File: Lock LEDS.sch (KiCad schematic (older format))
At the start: 9 parts

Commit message: Schematic completed first draft
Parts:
- R? (x3): value 510 -> 1.8k
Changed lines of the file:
@@
 $Descr A4 11693 8268
 encoding utf-8
-Sheet 3 12
+Sheet 3 18
 Title ""
 Date ""
@@
 P 4050 3250
 F 0 "R?" V 3843 3250 50  0000 C CNN
-F 1 "510" V 3934 3250 50  0000 C CNN
+F 1 "1.8k" V 3934 3250 50  0000 C CNN
 F 2 "" V 3980 3250 50  0001 C CNN
 F 3 "~" H 4050 3250 50  0001 C CNN
@@
 P 4050 3750
 F 0 "R?" V 3843 3750 50  0000 C CNN
-F 1 "510" V 3934 3750 50  0000 C CNN
+F 1 "1.8k" V 3934 3750 50  0000 C CNN
 F 2 "" V 3980 3750 50  0001 C CNN
 F 3 "~" H 4050 3750 50  0001 C CNN
@@
 P 4050 4250
 F 0 "R?" V 3843 4250 50  0000 C CNN
-F 1 "510" V 3934 4250 50  0000 C CNN
+F 1 "1.8k" V 3934 4250 50  0000 C CNN
 F 2 "" V 3980 4250 50  0001 C CNN
 F 3 "~" H 4050 4250 50  0001 C CNN

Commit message: Fixed PISO Shift Register Wiring
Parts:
- D? (x3): footprint (none) -> LED_SMD:LED_1206_3216Metric_ReverseMount_Hole1.8x2.4mm
- R? (x3): footprint (none) -> Resistor_SMD:R_1206_3216Metric_Pad1.42x1.75mm_HandSolder
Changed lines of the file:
@@
 F 0 "D?" H 4743 2995 50  0000 C CNN
 F 1 "NUM LOCK" H 4743 3086 50  0000 C CNN
-F 2 "" H 4750 3250 50  0001 C CNN
+F 2 "LED_SMD:LED_1206_3216Metric_ReverseMount_Hole1.8x2.4mm" H 4750 3250 50  0001 C CNN
 F 3 "~" H 4750 3250 50  0001 C CNN
 	1    4750 3250
@@
 F 0 "D?" H 4743 3495 50  0000 C CNN
 F 1 "CAPS LOCK" H 4743 3586 50  0000 C CNN
-F 2 "" H 4750 3750 50  0001 C CNN
+F 2 "LED_SMD:LED_1206_3216Metric_ReverseMount_Hole1.8x2.4mm" H 4750 3750 50  0001 C CNN
 F 3 "~" H 4750 3750 50  0001 C CNN
 	1    4750 3750
@@
 F 0 "D?" H 4743 3995 50  0000 C CNN
 F 1 "SCROLL LOCK" H 4743 4086 50  0000 C CNN
-F 2 "" H 4750 4250 50  0001 C CNN
+F 2 "LED_SMD:LED_1206_3216Metric_ReverseMount_Hole1.8x2.4mm" H 4750 4250 50  0001 C CNN
 F 3 "~" H 4750 4250 50  0001 C CNN
 	1    4750 4250
@@
 F 0 "R?" V 3843 3250 50  0000 C CNN
 F 1 "1.8k" V 3934 3250 50  0000 C CNN
-F 2 "" V 3980 3250 50  0001 C CNN
+F 2 "Resistor_SMD:R_1206_3216Metric_Pad1.42x1.75mm_HandSolder" V 3980 3250 50  0001 C CNN
 F 3 "~" H 4050 3250 50  0001 C CNN
 	1    4050 3250
@@
 F 0 "R?" V 3843 3750 50  0000 C CNN
 F 1 "1.8k" V 3934 3750 50  0000 C CNN
-F 2 "" V 3980 3750 50  0001 C CNN
+F 2 "Resistor_SMD:R_1206_3216Metric_Pad1.42x1.75mm_HandSolder" V 3980 3750 50  0001 C CNN
 F 3 "~" H 4050 3750 50  0001 C CNN
 	1    4050 3750
@@
 F 0 "R?" V 3843 4250 50  0000 C CNN
 F 1 "1.8k" V 3934 4250 50  0000 C CNN
-F 2 "" V 3980 4250 50  0001 C CNN
+F 2 "Resistor_SMD:R_1206_3216Metric_Pad1.42x1.75mm_HandSolder" V 3980 4250 50  0001 C CNN
 F 3 "~" H 4050 4250 50  0001 C CNN
 	1    4050 4250

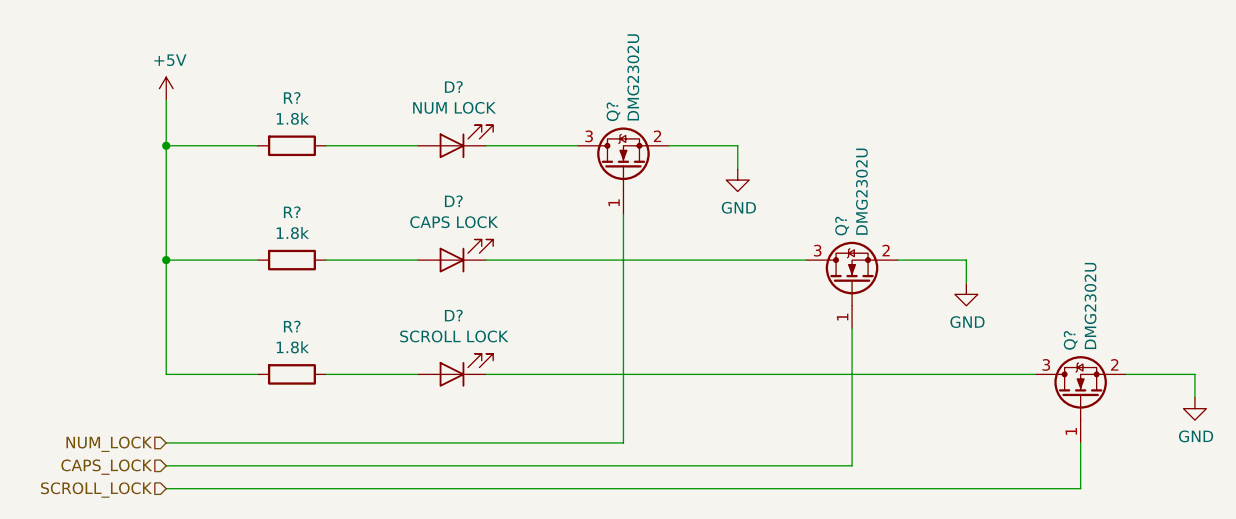
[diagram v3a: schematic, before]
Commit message: Corrected errors found in design rule check
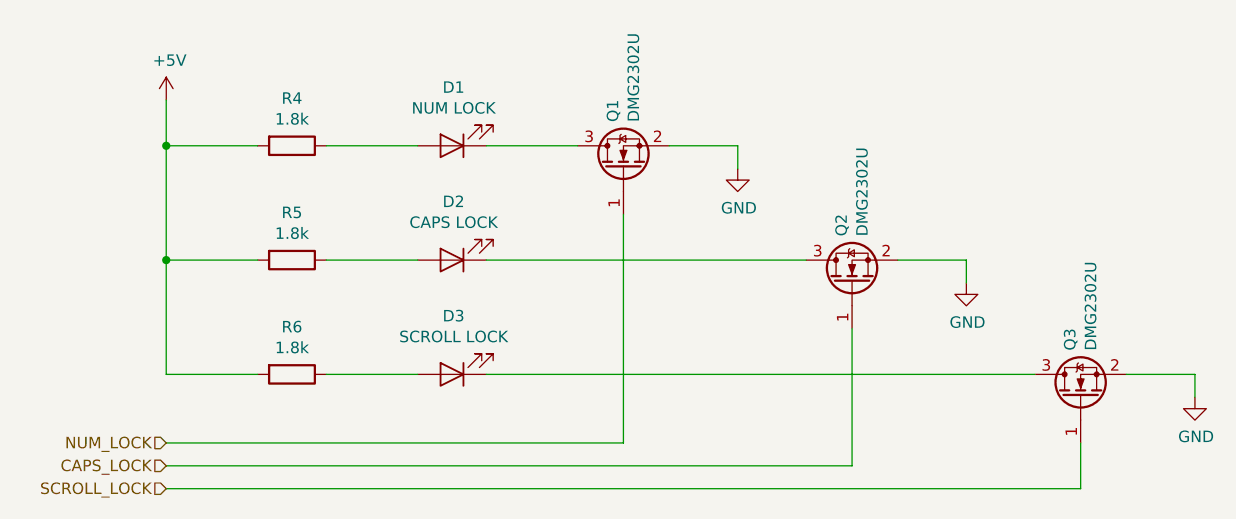
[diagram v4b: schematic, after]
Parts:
- gave numbers to parts that had none: 9
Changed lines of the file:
@@
 $EndDescr
 $Comp
-L Device:LED D?
+L Device:LED D1
 U 1 1 5EA55423
 P 4750 3250
-F 0 "D?" H 4743 2995 50  0000 C CNN
+F 0 "D1" H 4743 2995 50  0000 C CNN
 F 1 "NUM LOCK" H 4743 3086 50  0000 C CNN
 F 2 "LED_SMD:LED_1206_3216Metric_ReverseMount_Hole1.8x2.4mm" H 4750 3250 50  0001 C CNN
@@
 $EndComp
 $Comp
-L Device:LED D?
+L Device:LED D2
 U 1 1 5EA567AA
 P 4750 3750
-F 0 "D?" H 4743 3495 50  0000 C CNN
+F 0 "D2" H 4743 3495 50  0000 C CNN
 F 1 "CAPS LOCK" H 4743 3586 50  0000 C CNN
 F 2 "LED_SMD:LED_1206_3216Metric_ReverseMount_Hole1.8x2.4mm" H 4750 3750 50  0001 C CNN
@@
 $EndComp
 $Comp
-L Device:LED D?
+L Device:LED D3
 U 1 1 5EA569E5
 P 4750 4250
-F 0 "D?" H 4743 3995 50  0000 C CNN
+F 0 "D3" H 4743 3995 50  0000 C CNN
 F 1 "SCROLL LOCK" H 4743 4086 50  0000 C CNN
 F 2 "LED_SMD:LED_1206_3216Metric_ReverseMount_Hole1.8x2.4mm" H 4750 4250 50  0001 C CNN
@@
 $EndComp
 $Comp
-L Device:R R?
+L Device:R R4
 U 1 1 5EA5759E
 P 4050 3250
-F 0 "R?" V 3843 3250 50  0000 C CNN
+F 0 "R4" V 3843 3250 50  0000 C CNN
 F 1 "1.8k" V 3934 3250 50  0000 C CNN
 F 2 "Resistor_SMD:R_1206_3216Metric_Pad1.42x1.75mm_HandSolder" V 3980 3250 50  0001 C CNN
@@
 $EndComp
 $Comp
-L Device:R R?
+L Device:R R5
 U 1 1 5EA577A5
 P 4050 3750
-F 0 "R?" V 3843 3750 50  0000 C CNN
+F 0 "R5" V 3843 3750 50  0000 C CNN
 F 1 "1.8k" V 3934 3750 50  0000 C CNN
 F 2 "Resistor_SMD:R_1206_3216Metric_Pad1.42x1.75mm_HandSolder" V 3980 3750 50  0001 C CNN
@@
 $EndComp
 $Comp
-L Device:R R?
+L Device:R R6
 U 1 1 5EA57854
 P 4050 4250
-F 0 "R?" V 3843 4250 50  0000 C CNN
+F 0 "R6" V 3843 4250 50  0000 C CNN
 F 1 "1.8k" V 3934 4250 50  0000 C CNN
 F 2 "Resistor_SMD:R_1206_3216Metric_Pad1.42x1.75mm_HandSolder" V 3980 4250 50  0001 C CNN
@@
 	4200 4250 4600 4250
 $Comp
-L Transistor_FET:DMG2302U Q?
+L Transistor_FET:DMG2302U Q1
 U 1 1 5EA58235
 P 5500 3350
-F 0 "Q?" H 5704 3396 50  0000 L CNN
+F 0 "Q1" H 5704 3396 50  0000 L CNN
 F 1 "DMG2302U" H 5704 3305 50  0000 L CNN
 F 2 "Package_TO_SOT_SMD:SOT-23" H 5700 3275 50  0001 L CIN
@@
 $EndComp
 $Comp
-L Transistor_FET:DMG2302U Q?
+L Transistor_FET:DMG2302U Q2
 U 1 1 5EA70E5F
 P 6500 3850
-F 0 "Q?" H 6704 3896 50  0000 L CNN
+F 0 "Q2" H 6704 3896 50  0000 L CNN
 F 1 "DMG2302U" H 6704 3805 50  0000 L CNN
 F 2 "Package_TO_SOT_SMD:SOT-23" H 6700 3775 50  0001 L CIN
@@
 $EndComp
 $Comp
-L Transistor_FET:DMG2302U Q?
+L Transistor_FET:DMG2302U Q3
 U 1 1 5EA792B6
 P 7500 4350
-F 0 "Q?" H 7704 4396 50  0000 L CNN
+F 0 "Q3" H 7704 4396 50  0000 L CNN
 F 1 "DMG2302U" H 7704 4305 50  0000 L CNN
 F 2 "Package_TO_SOT_SMD:SOT-23" H 7700 4275 50  0001 L CIN
@@
 	8000 4250 8000 4350
 $Comp
-L power:GND #PWR?
+L power:GND #PWR023
 U 1 1 5EA91069
 P 6000 3350
-F 0 "#PWR?" H 6000 3100 50  0001 C CNN
+F 0 "#PWR023" H 6000 3100 50  0001 C CNN
 F 1 "GND" H 6005 3177 50  0000 C CNN
 F 2 "" H 6000 3350 50  0001 C CNN
@@
 	7000 3750 7000 3850
 $Comp
-L power:GND #PWR?
+L power:GND #PWR024
 U 1 1 5EA925AF
 P 7000 3850
-F 0 "#PWR?" H 7000 3600 50  0001 C CNN
+F 0 "#PWR024" H 7000 3600 50  0001 C CNN
 F 1 "GND" H 7005 3677 50  0000 C CNN
 F 2 "" H 7000 3850 50  0001 C CNN
@@
 $EndComp
 $Comp
-L power:GND #PWR?
+L power:GND #PWR025
 U 1 1 5EA9263A
 P 8000 4350
-F 0 "#PWR?" H 8000 4100 50  0001 C CNN
+F 0 "#PWR025" H 8000 4100 50  0001 C CNN
 F 1 "GND" H 8005 4177 50  0000 C CNN
 F 2 "" H 8000 4350 50  0001 C CNN
@@
 Connection ~ 3500 3250
 $Comp
-L power:+5V #PWR?
+L power:+5V #PWR022
 U 1 1 5EA9629E
 P 3500 3050
-F 0 "#PWR?" H 3500 2900 50  0001 C CNN
+F 0 "#PWR022" H 3500 2900 50  0001 C CNN
 F 1 "+5V" H 3515 3223 50  0000 C CNN
 F 2 "" H 3500 3050 50  0001 C CNN

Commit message: Redesigned for single large PCB
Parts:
- D1, D2, D3: footprint LED_SMD:LED_1206_3216Metric_ReverseMount_Hole1.8x2.4mm -> LED_SMD:LED_1206_3216Metric_Pad1.42x1.75mm_HandSolder
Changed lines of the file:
@@
 $Descr A4 11693 8268
 encoding utf-8
-Sheet 3 18
+Sheet 3 14
 Title ""
 Date ""
@@
 F 0 "D1" H 4743 2995 50  0000 C CNN
 F 1 "NUM LOCK" H 4743 3086 50  0000 C CNN
-F 2 "LED_SMD:LED_1206_3216Metric_ReverseMount_Hole1.8x2.4mm" H 4750 3250 50  0001 C CNN
+F 2 "LED_SMD:LED_1206_3216Metric_Pad1.42x1.75mm_HandSolder" H 4750 3250 50  0001 C CNN
 F 3 "~" H 4750 3250 50  0001 C CNN
 	1    4750 3250
@@
 F 0 "D2" H 4743 3495 50  0000 C CNN
 F 1 "CAPS LOCK" H 4743 3586 50  0000 C CNN
-F 2 "LED_SMD:LED_1206_3216Metric_ReverseMount_Hole1.8x2.4mm" H 4750 3750 50  0001 C CNN
+F 2 "LED_SMD:LED_1206_3216Metric_Pad1.42x1.75mm_HandSolder" H 4750 3750 50  0001 C CNN
 F 3 "~" H 4750 3750 50  0001 C CNN
 	1    4750 3750
@@
 F 0 "D3" H 4743 3995 50  0000 C CNN
 F 1 "SCROLL LOCK" H 4743 4086 50  0000 C CNN
-F 2 "LED_SMD:LED_1206_3216Metric_ReverseMount_Hole1.8x2.4mm" H 4750 4250 50  0001 C CNN
+F 2 "LED_SMD:LED_1206_3216Metric_Pad1.42x1.75mm_HandSolder" H 4750 4250 50  0001 C CNN
 F 3 "~" H 4750 4250 50  0001 C CNN
 	1    4750 4250

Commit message: PCB Routed, minor circuit changes
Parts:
- D1, D2, D3: footprint LED_SMD:LED_1206_3216Metric_Pad1.42x1.75mm_HandSolder -> LED_SMD:LED_1206_3216Metric_ReverseMount_Hole1.8x2.4mm
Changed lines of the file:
@@
 F 0 "D1" H 4743 2995 50  0000 C CNN
 F 1 "NUM LOCK" H 4743 3086 50  0000 C CNN
-F 2 "LED_SMD:LED_1206_3216Metric_Pad1.42x1.75mm_HandSolder" H 4750 3250 50  0001 C CNN
+F 2 "LED_SMD:LED_1206_3216Metric_ReverseMount_Hole1.8x2.4mm" H 4750 3250 50  0001 C CNN
 F 3 "~" H 4750 3250 50  0001 C CNN
 	1    4750 3250
@@
 F 0 "D2" H 4743 3495 50  0000 C CNN
 F 1 "CAPS LOCK" H 4743 3586 50  0000 C CNN
-F 2 "LED_SMD:LED_1206_3216Metric_Pad1.42x1.75mm_HandSolder" H 4750 3750 50  0001 C CNN
+F 2 "LED_SMD:LED_1206_3216Metric_ReverseMount_Hole1.8x2.4mm" H 4750 3750 50  0001 C CNN
 F 3 "~" H 4750 3750 50  0001 C CNN
 	1    4750 3750
@@
 F 0 "D3" H 4743 3995 50  0000 C CNN
 F 1 "SCROLL LOCK" H 4743 4086 50  0000 C CNN
-F 2 "LED_SMD:LED_1206_3216Metric_Pad1.42x1.75mm_HandSolder" H 4750 4250 50  0001 C CNN
+F 2 "LED_SMD:LED_1206_3216Metric_ReverseMount_Hole1.8x2.4mm" H 4750 4250 50  0001 C CNN
 F 3 "~" H 4750 4250 50  0001 C CNN
 	1    4750 4250
